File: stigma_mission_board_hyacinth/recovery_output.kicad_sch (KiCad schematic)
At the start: 15 parts, among them Q2 DMN2056U, Q3 AOSP21321, U13 INA181

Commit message: added some 3d models
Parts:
- J10: value ~ -> 43045-0400; footprint Connector_Molex:Molex_Micro-Fit_3.0_43045-0400_2x02_P3.00mm_Horizontal -> stigma:Molex_Micro-Fit_3.0_43045-0400_2x02_P3.00mm_Horizontal
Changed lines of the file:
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@@
 			)
 		)
-		(property "Value" "~"
+		(property "Value" "43045-0400"
 			(at 137.414 113.284 0)
 			(effects
@@
 			)
 		)
-		(property "Footprint" "Connector_Molex:Molex_Micro-Fit_3.0_43045-0400_2x02_P3.00mm_Horizontal"
+		(property "Footprint" "stigma:Molex_Micro-Fit_3.0_43045-0400_2x02_P3.00mm_Horizontal"
 			(at 140.97 113.03 0)
 			(effects
@@
 			)
 		)
-		(property "Datasheet" ""
+		(property "Datasheet" "https://www.mouser.de/ProductDetail/Molex/43045-0400?qs=UeCeOHRHQeaIqmxE9Bxdrw%3D%3D#:~:text=Datenblatt%3A-,43045%2D0400%20Datenblatt,-ECAD%20Model%3A"
 			(at 140.97 113.03 0)
 			(effects
@@
 			)
 		)
-		(property "Description" ""
+		(property "Description" "43045-0400"
 			(at 140.97 113.03 0)
 			(effects

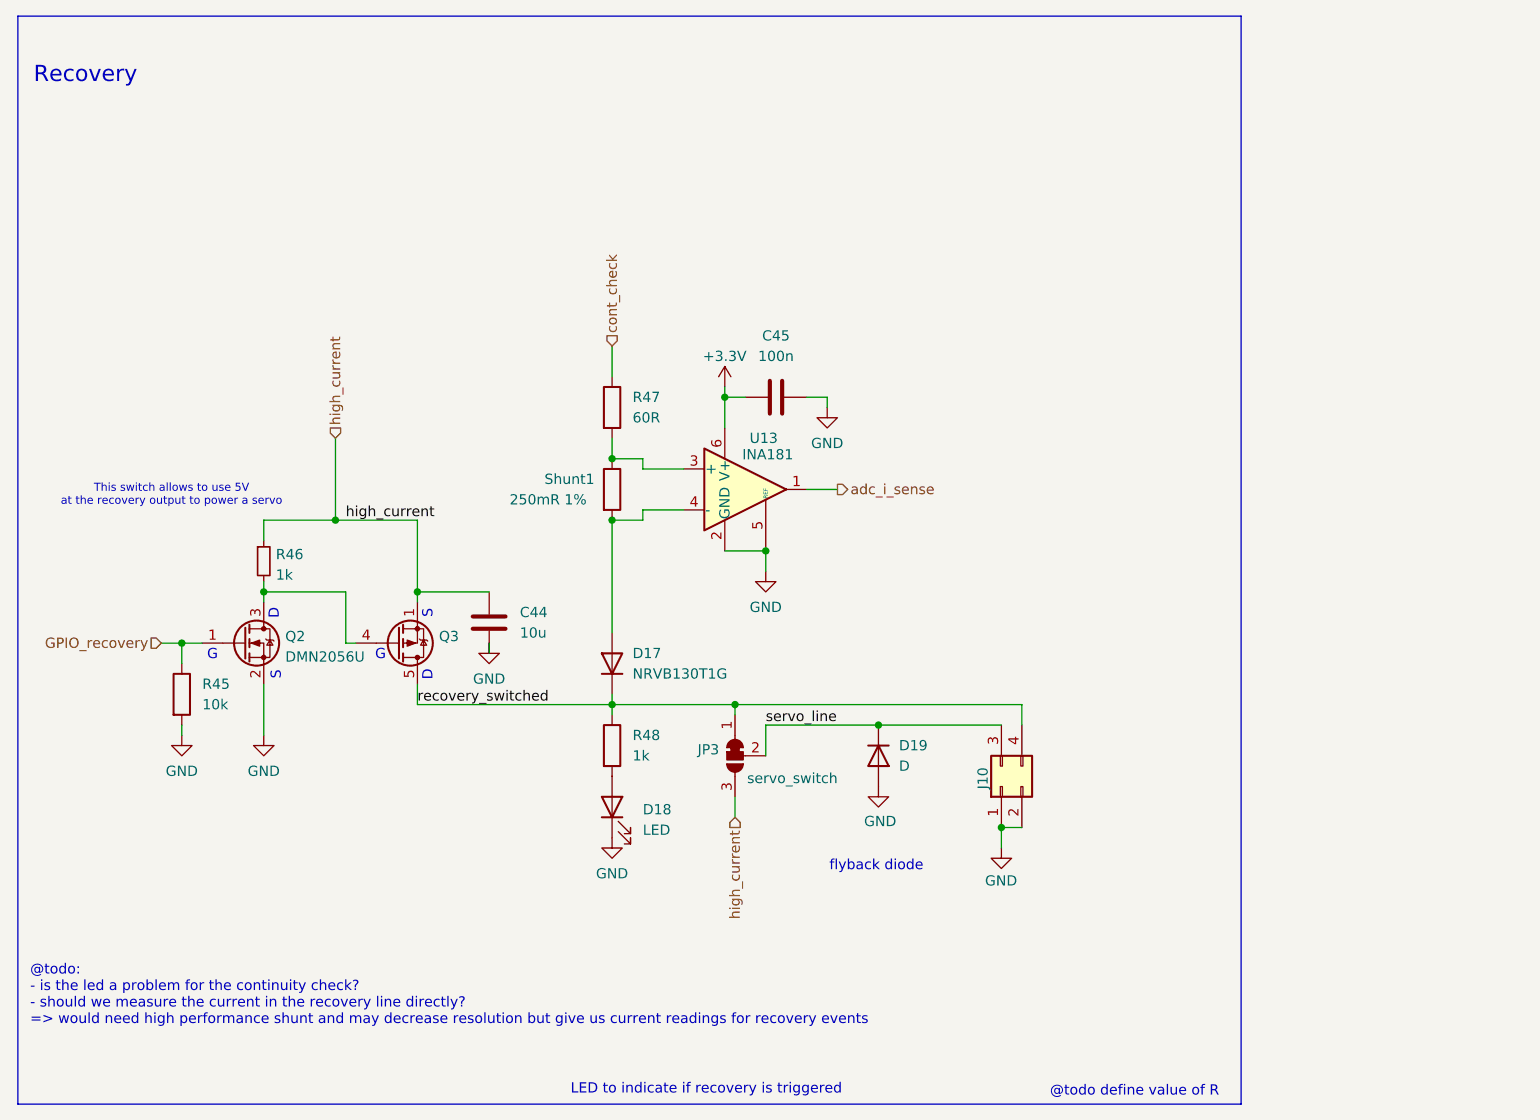
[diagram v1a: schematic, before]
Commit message: Rework recovery outputs to 2x2 low side
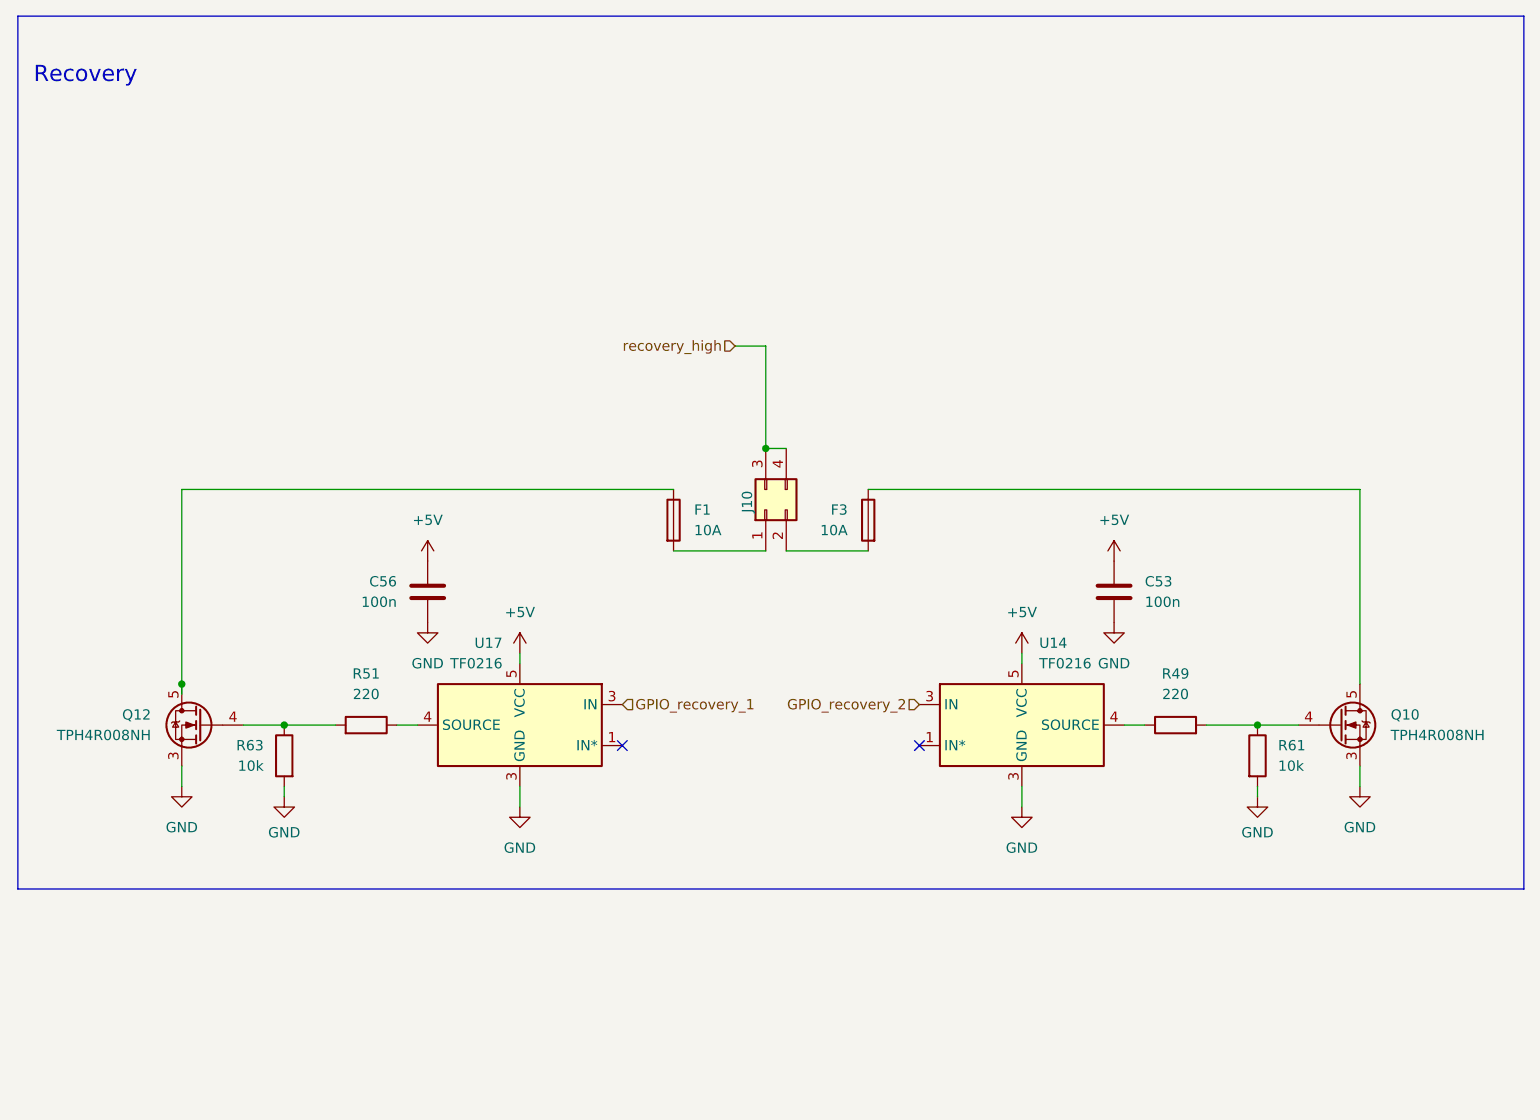
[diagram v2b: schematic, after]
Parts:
- removed C44: 10u, Capacitor_SMD:C_1206_3216Metric, symbol Device:C
- removed C45: 100n, Capacitor_SMD:C_0603_1608Metric, symbol Device:C
- removed D17: NRVB130T1G, Diode_SMD:D_SOD-123, symbol Device:D
- removed D18: LED, LED_SMD:LED_0603_1608Metric, symbol Device:LED
- removed D19: D, Diode_SMD:D_0603_1608Metric, symbol Device:D
- removed JP3: servo_switch, Stigma:SolderJumper-3_Open_RoundedPad2x2mm, symbol Jumper:SolderJumper_3_Bridged12
- removed Q2: DMN2056U, Package_TO_SOT_SMD:SOT-23, symbol Transistor_FET:DMG2302U
- removed Q3: AOSP21321, Package_SO:SO-8_3.9x4.9mm_P1.27mm, symbol euroc_fc:AOSP21321
- removed R45: 10k, Resistor_SMD:R_0603_1608Metric, symbol Device:R
- removed R46: 1k, Resistor_SMD:R_0603_1608Metric, symbol Device:R_Small
- removed R47: 60R, Resistor_SMD:R_0603_1608Metric, symbol Device:R
- removed R48: 1k, Resistor_SMD:R_0603_1608Metric, symbol Device:R
- removed Shunt1: 250mR 1%, Resistor_SMD:R_0805_2012Metric, symbol Device:R
- removed U13: INA181, Package_TO_SOT_SMD:SOT-23-6, symbol Amplifier_Current:INA181
- added C53, C56: 100n, Capacitor_SMD:C_0603_1608Metric, symbol Device:C
- added F1, F3: 10A, Fuse:Fuse_1206_3216Metric, symbol Device:Fuse
- added Q10, Q12: TPH4R008NH, Package_SO:SSOP-8_5.25x5.24mm_P1.27mm, symbol Transistor_FET:DMG2302U
- added R49, R51: 220, symbol Device:R
- added R61, R63: 10k, Resistor_SMD:R_0603_1608Metric, symbol Device:R
- added U14, U17: TF0216, Package_TO_SOT_SMD:SOT-23-5, symbol Driver_FET:ZXGD3003E6
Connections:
- net servo_line is gone; now on net recovery_high: J10.3 (Pin_3)
- net GND: now also C53.1, C56.1, Q10.3 (S), Q12.3 (S), R61.2, R63.2, U14.3 (GND), U17.3 (GND); no longer J10.1 (Pin_1), J10.2 (Pin_2)
- net recovery_switched renamed recovery_high
- new net: F3.1, Q10.5 (D)
- new net: F3.2, J10.2 (Pin_2)
- new net: F1.2, J10.1 (Pin_1)
- new net: R49.1, U14.4 (SOURCE)
- new net: Q10.4 (G), R49.2, R61.1
- new net: F1.1, Q12.5 (D)
- new net: Q12.4 (G), R51.2, R63.1
- new net: R51.1, U17.4 (SOURCE)
- new net +5V: C53.2, C56.2, U14.5 (VCC), U17.5 (VCC)
- new net GPIO_recovery_1: U17.3 (GND)
- new net GPIO_recovery_2: U14.3 (GND)
- no-connect marks 0 -> 2
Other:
- note removed: "@todo define value of R"
- note removed: "@todo: - is the led a problem for the continuity check? - should we measure the current in the recovery line directly? => would need high performance shunt and may decrease resolution but give us current readings for recovery events"
- note removed: "D"
- note removed: "G"
- note removed: "LED to indicate if recovery is triggered"
- note removed: "S"
- note removed: "This switch allows to use 5V at the recovery output to power a servo"
- note removed: "flyback diode"
- moved on the sheet: J10

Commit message: Refactor schematic, esp. recovery outputs, prepare for final layout
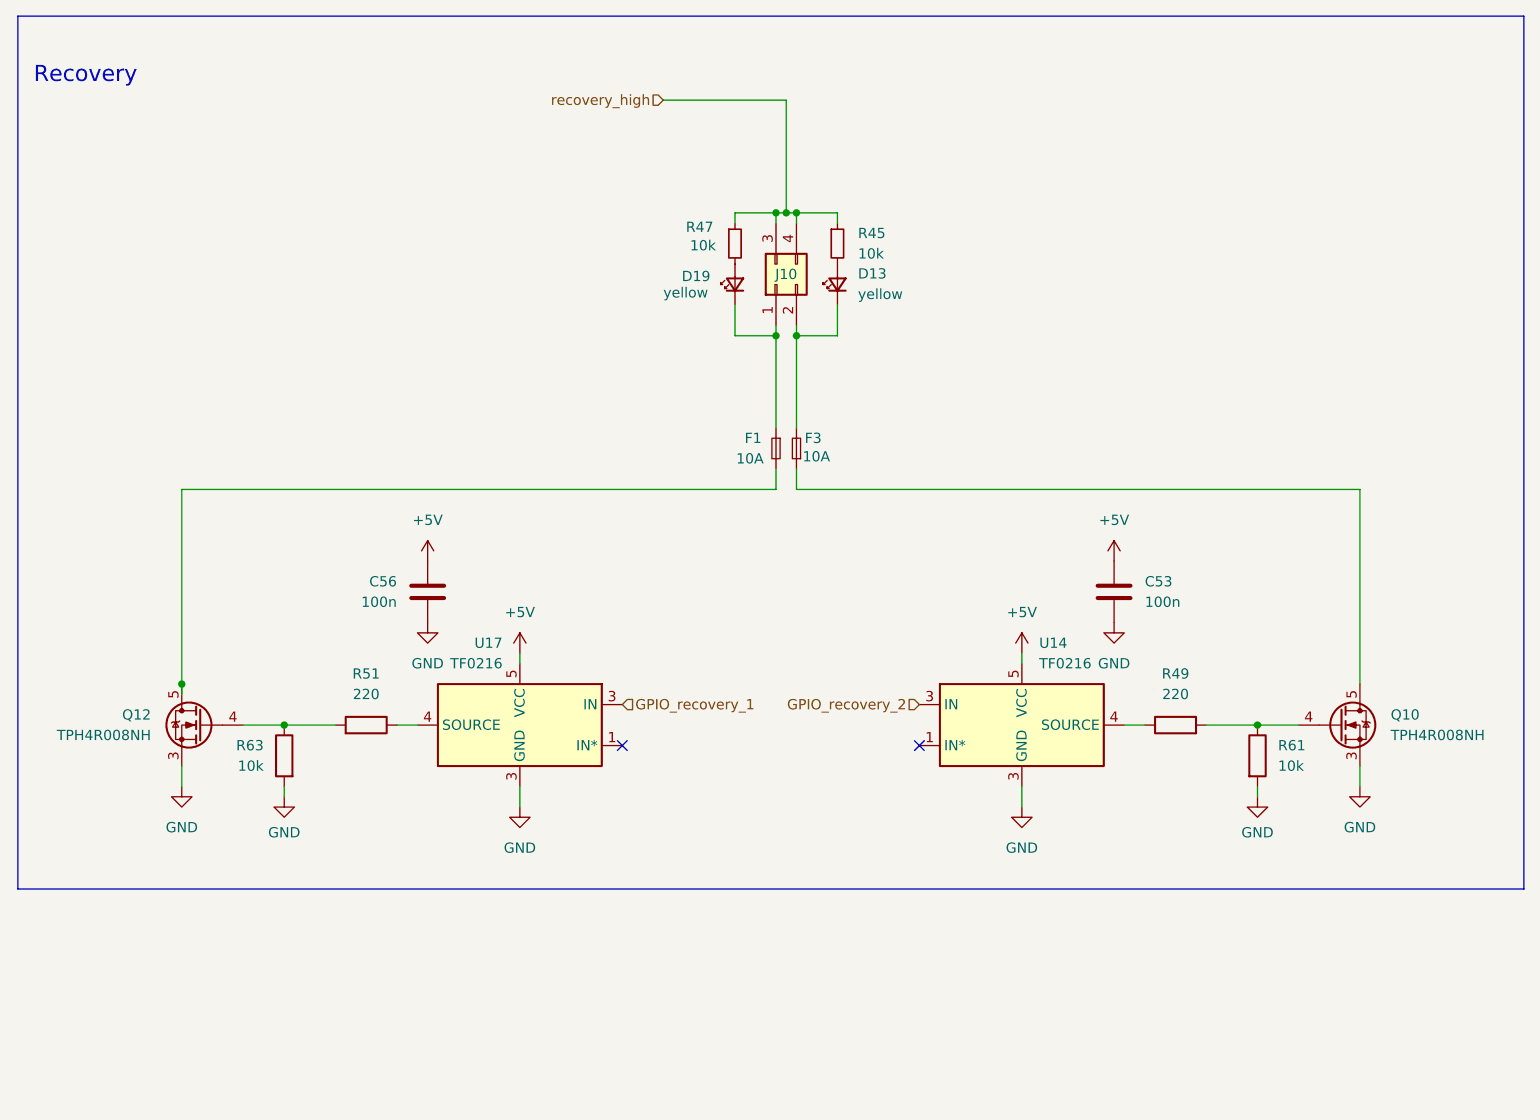
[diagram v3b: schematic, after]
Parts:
- added D13, D19: yellow, symbol Device:LED_Small
- added R45, R47: 10k, symbol Device:R_Small
- F1, F3: symbol Device:Fuse -> Device:Fuse_Small
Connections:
- net recovery_high: now also R45.1, R47.1
- net at F3.2, J10.2 (Pin_2): now also D13.1 (K)
- net at J10.1 (Pin_1): now also F1.1, D19.1 (K); no longer F1.2
- net at Q12.5 (D): now also F1.2; no longer F1.1
- new net: D19.2 (A), R47.2
- new net: D13.2 (A), R45.2
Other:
- moved on the sheet: F1, F3, J10
